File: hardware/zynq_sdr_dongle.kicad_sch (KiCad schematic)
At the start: 226 parts, among them J1 USB_C_Receptacle, J10 Conn_01x12_Male, J11 Conn_01x16_Male, J12 Conn_Coaxial, J13 Conn_01x04_Male, J2 USB_B_Micro, J3 Micro_SD_Card, J4 5024268012, J5 Conn_Coaxial, J6 Conn_Coaxial, J7 Conn_Coaxial, J8 Conn_Coaxial, J9 Conn_Coaxial, SW2 SW_DIP_x01, U1 DDR3, U10 TPS62088, U11 TPS2121, U2 xc7z010clg400, U3 AD9361, U4 TPS62088, U5 USB3346, U6 MAX38904C, U7 MAX38904C, U8 TPS62088, U9 TPS62088, X1 SiT1602B, Y1 Crystal_GND2

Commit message: Add USB ESD diode Revise DDR3 DQS0 polarity. ZYNQ can only be booted by SDIO which located MIO[40..45], correspondly change USB PHY MIO to MIO[28..39]. Add USB CC Control Logic Refactoring Schematic Transceiver Oscillator selected ZYNQ's configuration circuits and Oscillator selection Distribute transceiver's power
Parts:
- removed C1, C12, C6, C9: 18pF, Capacitor_SMD:C_0201_0603Metric, symbol Device:C
- removed C10, C13, C2, C22, C28, C29, C36, C62, C63, C78, C79: 0.1uF, Capacitor_SMD:C_0402_1005Metric, symbol Device:C_Small
- removed C100, C109, C11, C110, C111, C117, C14, C15, C16, C18, C19, C21, C24, C25, C26, C3, C31, C33, C34, C4, C5, C52, C53, C54, C55, C56, C57, C58, C59, C60, C61, C64, C65, C66, C67, C68, C69, C7, C70, C71, C72, C73, C74, C75, C76, C77, C8, C98, C99: 0.1uF, Capacitor_SMD:C_0201_0603Metric, symbol Device:C_Small
- removed C101, C102, C118, C119, C123, C128, C23, C27, C30, C32, C35, C37, C39, C40, C42, C43, C48, C49, C50, C51, C89, C90, C91, C92, C93, C94, C95, C96, C97: 4.7uF, Capacitor_SMD:C_0402_1005Metric, symbol Device:C
- removed C103, C106, C129: 1uF, Capacitor_SMD:C_0402_1005Metric, symbol Device:C
- removed C104, C105, C112, C113, C114, C82: NFM15PC146R0G3D, Capacitor_SMD_Local:C_0402_1005Metric, symbol Device:C_Feedthrough
- removed C107, C108, C115, C116, C130, C17, C20, C38, C44, C45, C46, C47, C80, C81, C83, C84, C85, C86, C87, C88: 0.1uF, Capacitor_SMD:C_0201_0603Metric, symbol Device:C
- removed C120, C124, C125, C41: 0.1uF, Capacitor_SMD:C_0402_1005Metric, symbol Device:C
- removed C121, C122, C126, C127: 10nF, Capacitor_SMD:C_0402_1005Metric, symbol Device:C
- removed FB1: FerriteBead_Small, Capacitor_SMD:C_0402_1005Metric, symbol Device:FerriteBead_Small
- removed FB2, FB3, FB4, FB5, FB6, FB7, FB8: FerriteBead_Small, Capacitor_SMD:C_0201_0603Metric, symbol Device:FerriteBead_Small
- removed FL1, FL2, FL3, FL4: 0850BM14E0016, RF_Converter:Balun_Johanson_1.6x0.8mm, symbol Filter:0850BM14E0016
- removed J1: USB_C_Receptacle, Connector_USB:USB_C_Receptacle_Amphenol_12401548E4-2A_CircularHoles, symbol Connector:USB_C_Receptacle
- removed J10: Conn_01x12_Male, Connector_PinHeader_2.54mm:PinHeader_1x12_P2.54mm_Vertical, symbol Connector:Conn_01x12_Male
- removed J12, J5, J6, J7, J8, J9: Conn_Coaxial, Connector_Coaxial_Local:U.FL_Molex_MCRF_73412-0110_Vertical, symbol Connector:Conn_Coaxial
- removed J13: Conn_01x04_Male, Connector_Local:BM03B-ACHSS-GAN-TF, symbol Connector:Conn_01x04_Male
- removed J2: USB_B_Micro, Connector_USB:USB_Micro-B_Amphenol_10104110_Horizontal, symbol Connector:USB_B_Micro
- removed J3: Micro_SD_Card, Connector_Card:microSD_HC_Molex_104031-0811, symbol Connector:Micro_SD_Card
- removed J4: 5024268012, Connector_Molex:Molex_SlimStack_502430-8010_2x40_P0.40mm_Vertical, symbol Connector_Generic:Conn_02x40_Odd_Even
- removed L1, L6, L7, L8: DFE18SANR47MG0, Inductor_SMD:L_Murata_LQH2MCNxxxx02_2.0x1.6mm, symbol pspice:INDUCTOR
- removed L2, L3, L4, L5: L, Inductor_SMD:L_0402_1005Metric, symbol Device:L
- removed R1, R4, R5: 80Ω, Resistor_SMD:R_0201_0603Metric, symbol Device:R
- removed R10: 18K, Resistor_SMD:R_0201_0603Metric, symbol Device:R
- removed R11, R12: 14.3K, Resistor_SMD:R_0201_0603Metric, symbol Device:R
- removed R13, R14, R15, R16, R17, R18, R23, R24, R29, R30, R37, R38, R39, R46, R6, R7: R, Resistor_SMD:R_0201_0603Metric, symbol Device:R
- removed R19, R22, R25, R8: 10K, Resistor_SMD:R_0201_0603Metric, symbol Device:R
- removed R2: 4K7Ω, Resistor_SMD:R_0201_0603Metric, symbol Device:R
- removed R20: 200K, Resistor_SMD:R_0201_0603Metric, symbol Device:R
- removed R21: 100K, Resistor_SMD:R_0201_0603Metric, symbol Device:R
- removed R26: 22K, Resistor_SMD:R_0201_0603Metric, symbol Device:R
- removed R27: 33K, Resistor_SMD:R_0201_0603Metric, symbol Device:R
- removed R28: 0R, Resistor_SMD:R_0201_0603Metric, symbol Device:R
- removed R3: 240Ω, Resistor_SMD:R_0201_0603Metric, symbol Device:R
- removed R31, R32, R33, R34, R35, R36, R40: 1K, Resistor_SMD:R_0201_0603Metric, symbol Device:R
- removed R41: 0R, Resistor_SMD:R_0402_1005Metric, symbol Device:R
- removed R9: 82K, Resistor_SMD:R_0201_0603Metric, symbol Device:R
- removed SW2: SW_DIP_x01, Switcher:EVQ9P701P, symbol Switch:SW_DIP_x01
- removed U1: DDR3, Package_BGA:BGA-96_9.0x13.0mm_Layout2x3x16_P0.8mm_NoPaste, symbol 7z010_ddr:AS4C256M16D3
- removed U10, U4, U8, U9: TPS62088, Package_CSP:WLCSP-6_1.4x1.0mm_P0.4mm, symbol Regulator_Switching_Local:TPS62088
- removed U11: TPS2121, Capacitor_SMD_Local:VQFN-12_2p0_2p5_0p5, symbol Load_Switch_Local:TPS2121
- removed U2: xc7z010clg400, Package_BGA:Xilinx_CLG400_NoPaste_JLC_Package_Delay, symbol 7z010_ddr:xc7z010clg400
- removed U3: AD9361, RF_Transceiver:bga-100_10_10_1p32_0p8, symbol Transceiver:AD9361
- removed U5: USB3346, Package_DFN_QFN:QFN-24-1EP_4x4mm_P0.5mm_EP2.6x2.6mm, symbol Interface_USB:USB3346
- removed U6, U7: MAX38904C, Package_CSP_Local:wlp-15_2p168_1p338_0p5_0p4, symbol Power_Supervisor_Local:MAX38904C
- removed X1: SiT1602B, Oscillator:Oscillator_SMD_ECS_2520MV-xxx-xx-4Pin_2.5x2.0mm, symbol Oscillator:ECS-2520MV-xxx-xx
- removed Y1: Crystal_GND2, Oscillator:Oscillator_SMD_ECS_2520MV-xxx-xx-4Pin_2.5x2.0mm, symbol Device:Crystal_GND2
- added J10: Conn_01x13_Male, Connector_PinHeader_2.54mm:PinHeader_1x13_P2.54mm_Vertical, symbol Connector:Conn_01x13_Male
- added R54, R60, R61, R63: N/A, Resistor_SMD:R_0201_0603Metric, symbol Device:R
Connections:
- net +1V8 is gone; now on net +5V: D1.2 (A)
- net VCC_5V0_AUX is gone; now on net USB Connector/PWR_STA: R45.1
- net +3V3: now also J10.1 (Pin_1)
- net +5V: now also D2.1 (K)
- net ARD_ANALOG5: now also J11.8 (Pin_8), R60.1; no longer R42.1
- net ARD_AREF: now also R54.2, R63.2
- net FPGA_VREF: now also R54.1
- net GND: now also D3.2 (A), J10.2 (Pin_2); no longer D2.1 (K), D3.1 (K)
- net PS-SRST#: now also J10.3 (Pin_3)
- net PS_MIO10_SCL: now also J10.7 (Pin_7)
- net PS_MIO11_SDA: now also J10.6 (Pin_6)
- net TRANS_AUX_ADC: now also R61.2; no longer J11.10 (Pin_10)
- net TRANS_AUX_DAC1: no longer J11.9 (Pin_9)
- net TRANS_AUX_DAC2: now also R60.2; no longer J11.8 (Pin_8)
- net UART_RX: now also J10.5 (Pin_5)
- net UART_TX: now also J10.4 (Pin_4)
- net at R45.2: now also D3.1 (K); no longer D3.2 (A)
- net 5V_VBUS renamed USB Connector/PWR_STA
- new net ARD_ANALOG6: J11.9 (Pin_9), R42.1
- new net ARD_ANALOG7: J11.10 (Pin_10), R61.1
- new net PS_MIO16_SPI_CLK: J10.9 (Pin_9)
- new net PS_MIO17_SPI_MISO: J10.10 (Pin_10)
- new net PS_MIO18_SPI_SS: J10.11 (Pin_11)
- new net PS_MIO19_SPI_MOSI: J10.8 (Pin_8)
- new net PS_MIO20_SPI_SS1: J10.12 (Pin_12)
- new net PS_MIO21_SPI_SS2: J10.13 (Pin_13)
- new net ZYNQ PL Part/FPGA_SRCCN_Y8: R63.1
- no-connect marks 36 -> 0
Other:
- added sheet BTB Connector (BTB_Connector.kicad_sch)
- added sheet Power Manage (Power_Manage.kicad_sch)
- added sheet Transceiver Powr (Transceiver_Power.kicad_sch)
- added sheet Transceiver RF (Transceiver_RF.kicad_sch)
- added sheet USB Connector (USB_Connector.kicad_sch)
- added sheet ZYNQ PL Part (ZYNQ_PL.kicad_sch)
- added sheet ZYNQ PS Part (ZYNQ_PS.kicad_sch)
- note added: "Transceiver"
- note added: "ZYNQ"
- note added: "cannot fanout to ardruino IO"
- note removed: "1.8V"
- note removed: "Pullup by PS part"
- note removed: "VDDA_TX_LO"
- note removed: "这里有一个问题就是如果把这个DAC接到Pin上 这个Pin就没有DIO功能了"
- moved on the sheet: J11, R42

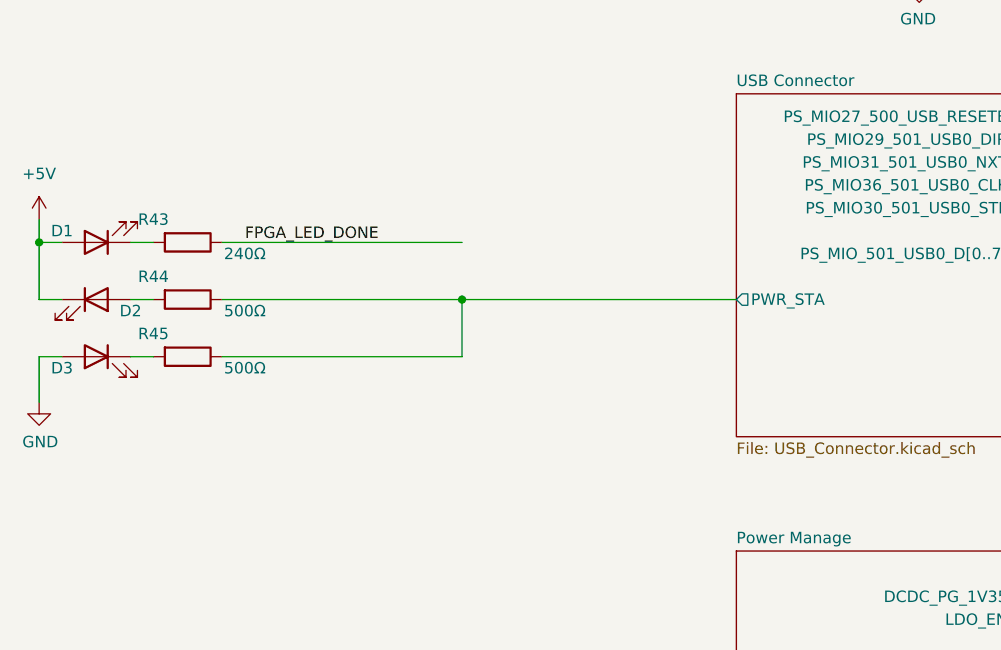
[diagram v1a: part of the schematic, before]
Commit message: add sdio level shift ciruit
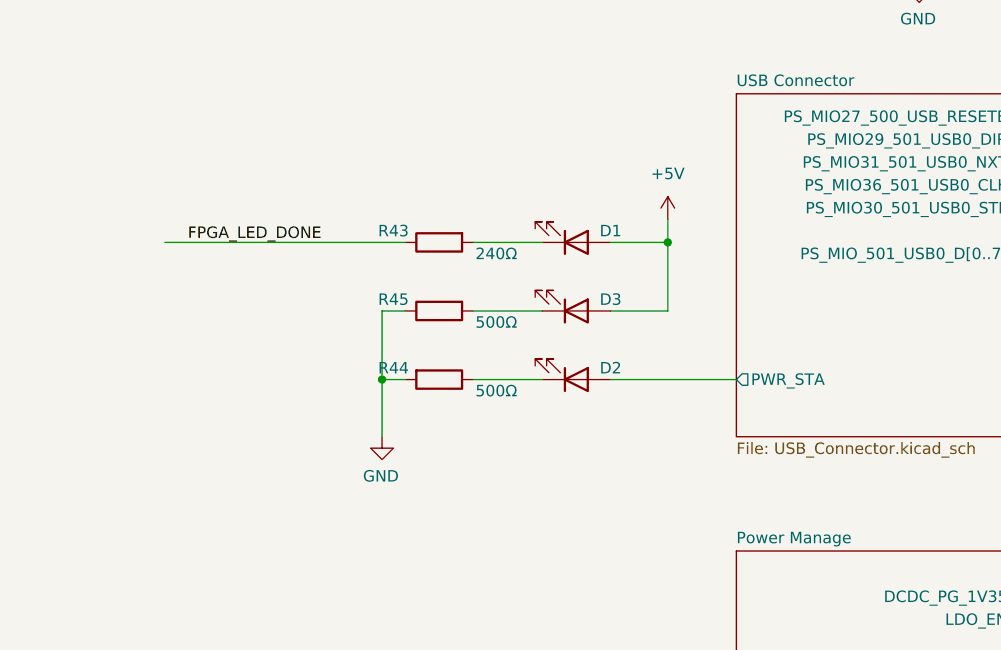
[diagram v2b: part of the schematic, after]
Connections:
- net +5V: now also D3.2 (A); no longer D2.1 (K)
- net GND: now also R44.2, R45.1; no longer D3.2 (A)
- net USB Connector/PWR_STA: now also D2.2 (A); no longer R44.1, R45.1
- new net: D2.1 (K), R44.1
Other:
- moved on the sheet: D1, D2, D3, R43, R44, R45
